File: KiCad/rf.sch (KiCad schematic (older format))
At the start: 19 parts

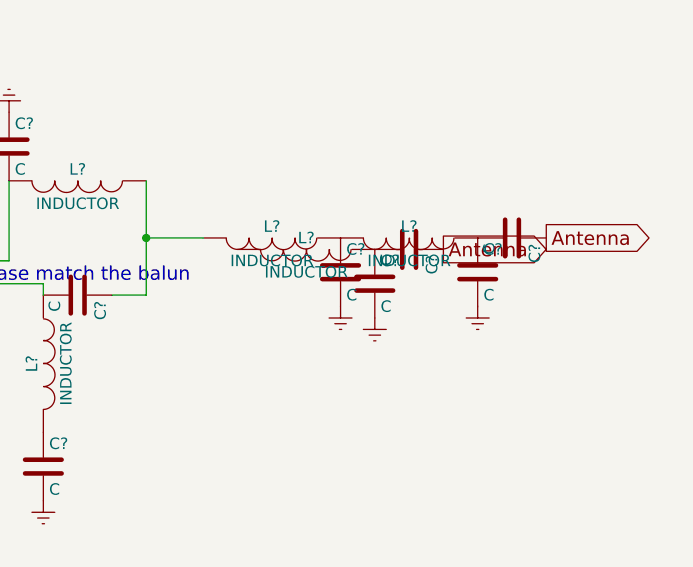
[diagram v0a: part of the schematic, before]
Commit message: Fixed a schematic error in the RF filter
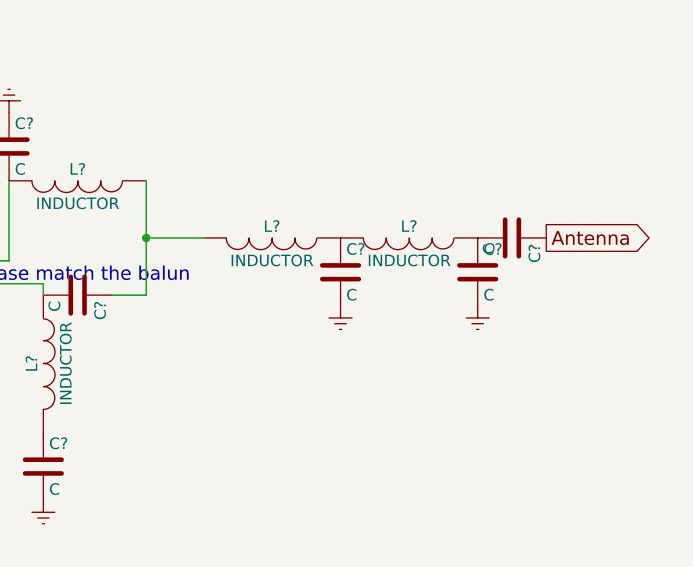
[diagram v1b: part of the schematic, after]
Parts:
- removed C? (x2): C, symbol C
- removed L?: INDUCTOR, symbol INDUCTOR
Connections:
- net at C?.2, L?.1: now also C?.1
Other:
- moved on the sheet: C?
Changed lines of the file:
@@
-$Comp
-L C C?
-U 1 1 580FADFC
-P 8400 3150
-F 0 "C?" H 8425 3250 50  0000 L CNN
-F 1 "C" H 8425 3050 50  0000 L CNN
-F 2 "" H 8438 3000 50  0000 C CNN
-F 3 "" H 8400 3150 50  0000 C CNN
-	1    8400 3150
-	1    0    0    -1
-$EndComp
 $Comp
 L C C?
@@
 	1    0    0    -1
 $EndComp
-$Comp
-L Earth #PWR025
-U 1 1 580FAE10
-P 8400 3300
-F 0 "#PWR025" H 8400 3050 50  0001 C CNN
-F 1 "Earth" H 8400 3150 50  0001 C CNN
-F 2 "" H 8400 3300 50  0000 C CNN
-F 3 "" H 8400 3300 50  0000 C CNN
-	1    8400 3300
-	1    0    0    -1
-$EndComp
 Text GLabel 8700 3000 2    60   Output ~ 0
 Antenna
@@
 Remember to phase match the balun
 $Comp
-L INDUCTOR L?
-U 1 1 58113EFE
-P 7650 3050
-F 0 "L?" V 7600 3050 50  0000 C CNN
-F 1 "INDUCTOR" V 7750 3050 50  0000 C CNN
-F 2 "" H 7650 3050 50  0000 C CNN
-F 3 "" H 7650 3050 50  0000 C CNN
-	1    7650 3050
-	0    1    1    0
-$EndComp
-$Comp
 L C C?
 U 1 1 58113F04
-P 7950 3200
-F 0 "C?" H 7975 3300 50  0000 L CNN
-F 1 "C" H 7975 3100 50  0000 L CNN
-F 2 "" H 7988 3050 50  0000 C CNN
-F 3 "" H 7950 3200 50  0000 C CNN
-	1    7950 3200
-	1    0    0    -1
-$EndComp
-$Comp
-L C C?
-U 1 1 58113F0A
-P 8100 3050
-F 0 "C?" H 8125 3150 50  0000 L CNN
-F 1 "C" H 8125 2950 50  0000 L CNN
-F 2 "" H 8138 2900 50  0000 C CNN
-F 3 "" H 8100 3050 50  0000 C CNN
-	1    8100 3050
-	0    1    1    0
+P 8400 3150
+F 0 "C?" H 8425 3250 50  0000 L CNN
+F 1 "C" H 8425 3050 50  0000 L CNN
+F 2 "" H 8438 3000 50  0000 C CNN
+F 3 "" H 8400 3150 50  0000 C CNN
+	1    8400 3150
+	1    0    0    -1
 $EndComp
 $Comp
 L Earth #PWR?
 U 1 1 58113F10
-P 7950 3350
-F 0 "#PWR?" H 7950 3100 50  0001 C CNN
-F 1 "Earth" H 7950 3200 50  0001 C CNN
-F 2 "" H 7950 3350 50  0000 C CNN
-F 3 "" H 7950 3350 50  0000 C CNN
-	1    7950 3350
-	1    0    0    -1
-$EndComp
-Text GLabel 8250 3050 2    60   Output ~ 0
-Antenna
+P 8400 3300
+F 0 "#PWR?" H 8400 3050 50  0001 C CNN
+F 1 "Earth" H 8400 3150 50  0001 C CNN
+F 2 "" H 8400 3300 50  0000 C CNN
+F 3 "" H 8400 3300 50  0000 C CNN
+	1    8400 3300
+	1    0    0    -1
+$EndComp
 $EndSCHEMATC

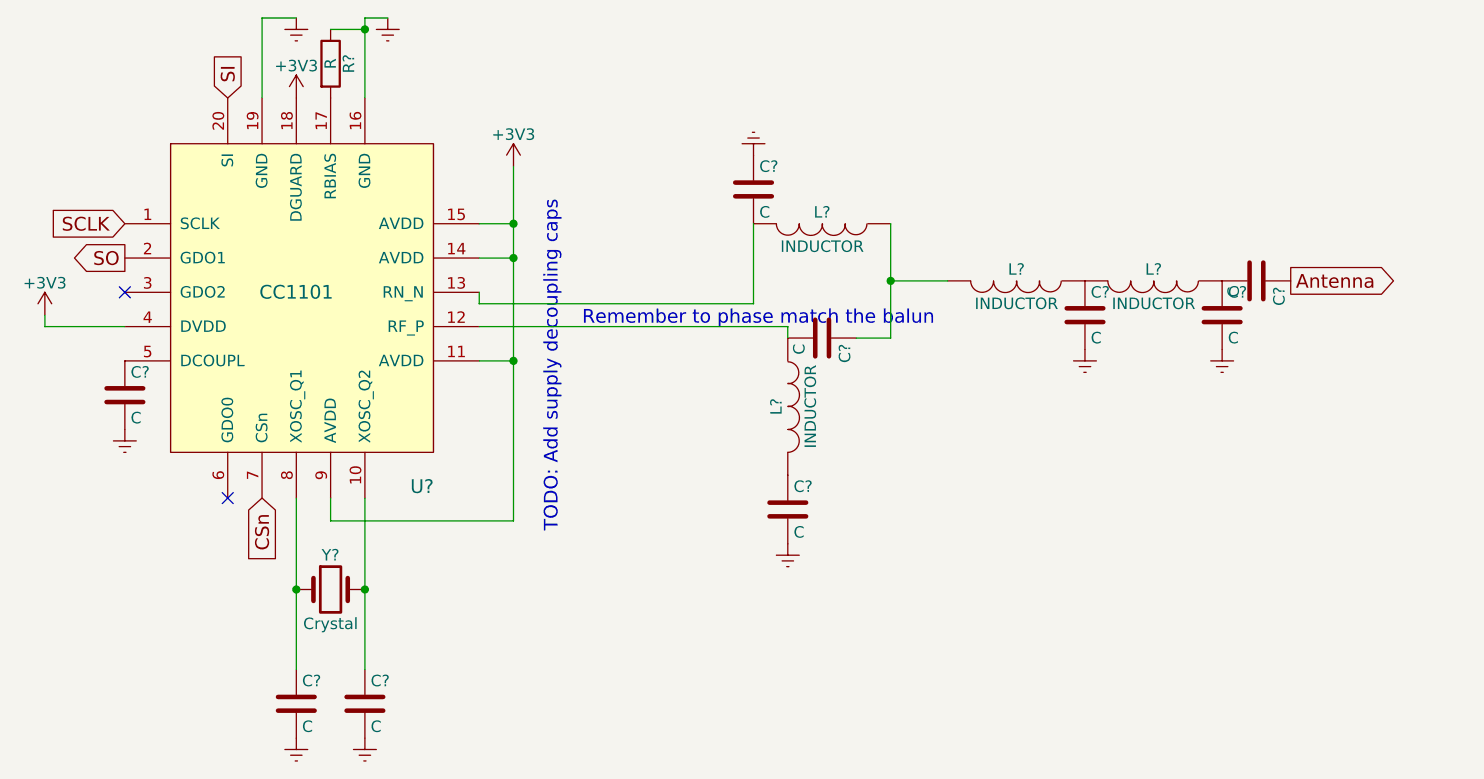
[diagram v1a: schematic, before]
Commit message: Added edge connector and UART leveler
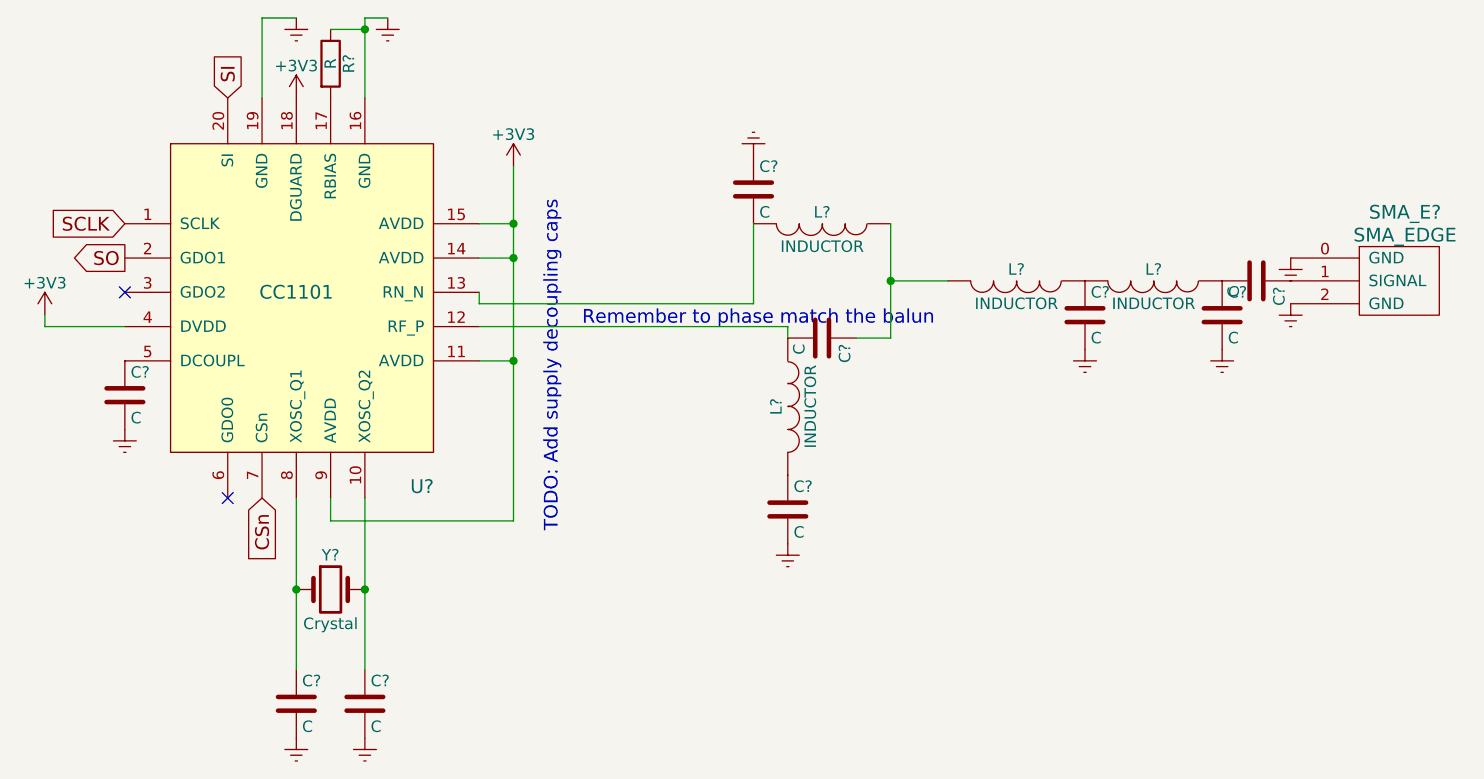
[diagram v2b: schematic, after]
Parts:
- added SMA_E?: SMA_EDGE, symbol SMA_EDGE
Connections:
- net Earth: now also SMA_E?.0 (GND), SMA_E?.2 (GND)
- net Antenna: no longer names the net of C?.1
- net Antenna: now also SMA_E?.1 (SIGNAL)
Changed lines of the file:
@@
 LIBS:Xicor
 LIBS:Zilog
+LIBS:sma_edge
 LIBS:cc1100-cache
 EELAYER 25 0
@@
 	1    0    0    -1
 $EndComp
-Text GLabel 8700 3000 2    60   Output ~ 0
-Antenna
 $Comp
 L CC1101 U?
@@
 $EndComp
 Wire Wire Line
-	6950 2750 6950 3250
+	6950 2750 6950 3000
+Wire Wire Line
+	6950 3000 6950 3250
 Connection ~ 6950 3000
 Wire Wire Line
@@
 	4200 1850 4350 1850
 Wire Wire Line
-	4650 1850 4650 2200
+	4650 1850 4650 1900
+Wire Wire Line
+	4650 1900 4650 2200
 Wire Wire Line
 	4650 1850 4750 1850
@@
 	5150 2750 5300 2750
 Wire Wire Line
-	5300 2500 5300 4050
+	5300 2500 5300 2750
+Wire Wire Line
+	5300 2750 5300 2900
+Wire Wire Line
+	5300 2900 5300 3350
+Wire Wire Line
+	5300 3350 5300 4050
 Wire Wire Line
 	5300 2900 5150 2900
@@
 $EndComp
 Wire Wire Line
-	4350 3950 4350 4700
+	4350 3950 4350 4350
+Wire Wire Line
+	4350 4350 4350 4700
 Connection ~ 4350 4350
 Wire Wire Line
-	4650 3950 4650 4700
+	4650 3950 4650 4350
+Wire Wire Line
+	4650 4350 4650 4700
 Connection ~ 4650 4350
 $Comp
@@
 	1    0    0    -1
 $EndComp
+$Comp
+L SMA_EDGE SMA_E?
+U 1 1 5814B7ED
+P 9050 3000
+F 0 "SMA_E?" H 9200 3300 60  0000 C CNN
+F 1 "SMA_EDGE" H 9200 3200 60  0000 C CNN
+F 2 "" H 9050 3000 60  0001 C CNN
+F 3 "" H 9050 3000 60  0001 C CNN
+	1    9050 3000
+	1    0    0    -1
+$EndComp
+$Comp
+L Earth #PWR?
+U 1 1 5814BBC3
+P 8700 3100
+F 0 "#PWR?" H 8700 2850 50  0001 C CNN
+F 1 "Earth" H 8700 2950 50  0001 C CNN
+F 2 "" H 8700 3100 50  0000 C CNN
+F 3 "" H 8700 3100 50  0000 C CNN
+	1    8700 3100
+	1    0    0    -1
+$EndComp
+$Comp
+L Earth #PWR?
+U 1 1 5814BC0A
+P 8700 2900
+F 0 "#PWR?" H 8700 2650 50  0001 C CNN
+F 1 "Earth" H 8700 2750 50  0001 C CNN
+F 2 "" H 8700 2900 50  0000 C CNN
+F 3 "" H 8700 2900 50  0000 C CNN
+	1    8700 2900
+	1    0    0    -1
+$EndComp

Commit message: Connected supply error pin
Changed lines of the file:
@@
 $EndComp
 Wire Wire Line
-	6950 2750 6950 3000
-Wire Wire Line
-	6950 3000 6950 3250
+	6950 2750 6950 3250
 Connection ~ 6950 3000
 Wire Wire Line
@@
 	4200 1850 4350 1850
 Wire Wire Line
-	4650 1850 4650 1900
-Wire Wire Line
-	4650 1900 4650 2200
+	4650 1850 4650 2200
 Wire Wire Line
 	4650 1850 4750 1850
@@
 	5150 2750 5300 2750
 Wire Wire Line
-	5300 2500 5300 2750
-Wire Wire Line
-	5300 2750 5300 2900
-Wire Wire Line
-	5300 2900 5300 3350
-Wire Wire Line
-	5300 3350 5300 4050
+	5300 2500 5300 4050
 Wire Wire Line
 	5300 2900 5150 2900
@@
 $EndComp
 Wire Wire Line
-	4350 3950 4350 4350
-Wire Wire Line
-	4350 4350 4350 4700
+	4350 3950 4350 4700
 Connection ~ 4350 4350
 Wire Wire Line
-	4650 3950 4650 4350
-Wire Wire Line
-	4650 4350 4650 4700
+	4650 3950 4650 4700
 Connection ~ 4650 4350
 $Comp

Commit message: KiCad Update and ALERT pull-up added
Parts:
- L? (x4): symbol INDUCTOR -> INDUCTOR-RESCUE-cc1100
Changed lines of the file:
@@
 EESchema Schematic File Version 2
+LIBS:cc1100-rescue
 LIBS:power
 LIBS:device
@@
 $EndDescr
 $Comp
-L INDUCTOR L?
+L INDUCTOR-RESCUE-cc1100 L?
 U 1 1 580FADB8
 P 6650 2750
+AR Path="/580FADB8" Ref="L?"  Part="1"
+AR Path="/580F9D89/580FADB8" Ref="L?"  Part="1"
 F 0 "L?" V 6600 2750 50  0000 C CNN
 F 1 "INDUCTOR" V 6750 2750 50  0000 C CNN
@@
 $EndComp
 $Comp
-L INDUCTOR L?
+L INDUCTOR-RESCUE-cc1100 L?
 U 1 1 580FADD3
 P 6500 3550
+AR Path="/580FADD3" Ref="L?"  Part="1"
+AR Path="/580F9D89/580FADD3" Ref="L?"  Part="1"
 F 0 "L?" V 6450 3550 50  0000 C CNN
 F 1 "INDUCTOR" V 6600 3550 50  0000 C CNN
@@
 $EndComp
 $Comp
-L INDUCTOR L?
+L INDUCTOR-RESCUE-cc1100 L?
 U 1 1 580FADE7
 P 7500 3000
+AR Path="/580FADE7" Ref="L?"  Part="1"
+AR Path="/580F9D89/580FADE7" Ref="L?"  Part="1"
 F 0 "L?" V 7450 3000 50  0000 C CNN
 F 1 "INDUCTOR" V 7600 3000 50  0000 C CNN
@@
 $EndComp
 $Comp
-L INDUCTOR L?
+L INDUCTOR-RESCUE-cc1100 L?
 U 1 1 580FADF5
 P 8100 3000
+AR Path="/580FADF5" Ref="L?"  Part="1"
+AR Path="/580F9D89/580FADF5" Ref="L?"  Part="1"
 F 0 "L?" V 8050 3000 50  0000 C CNN
 F 1 "INDUCTOR" V 8200 3000 50  0000 C CNN
